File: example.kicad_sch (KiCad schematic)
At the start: 3 parts, among them J1 SSD1309 24-Pin Connector, J2 SSD1322 30-Pin Connector, J3 SSD1327 16-Pin Connector

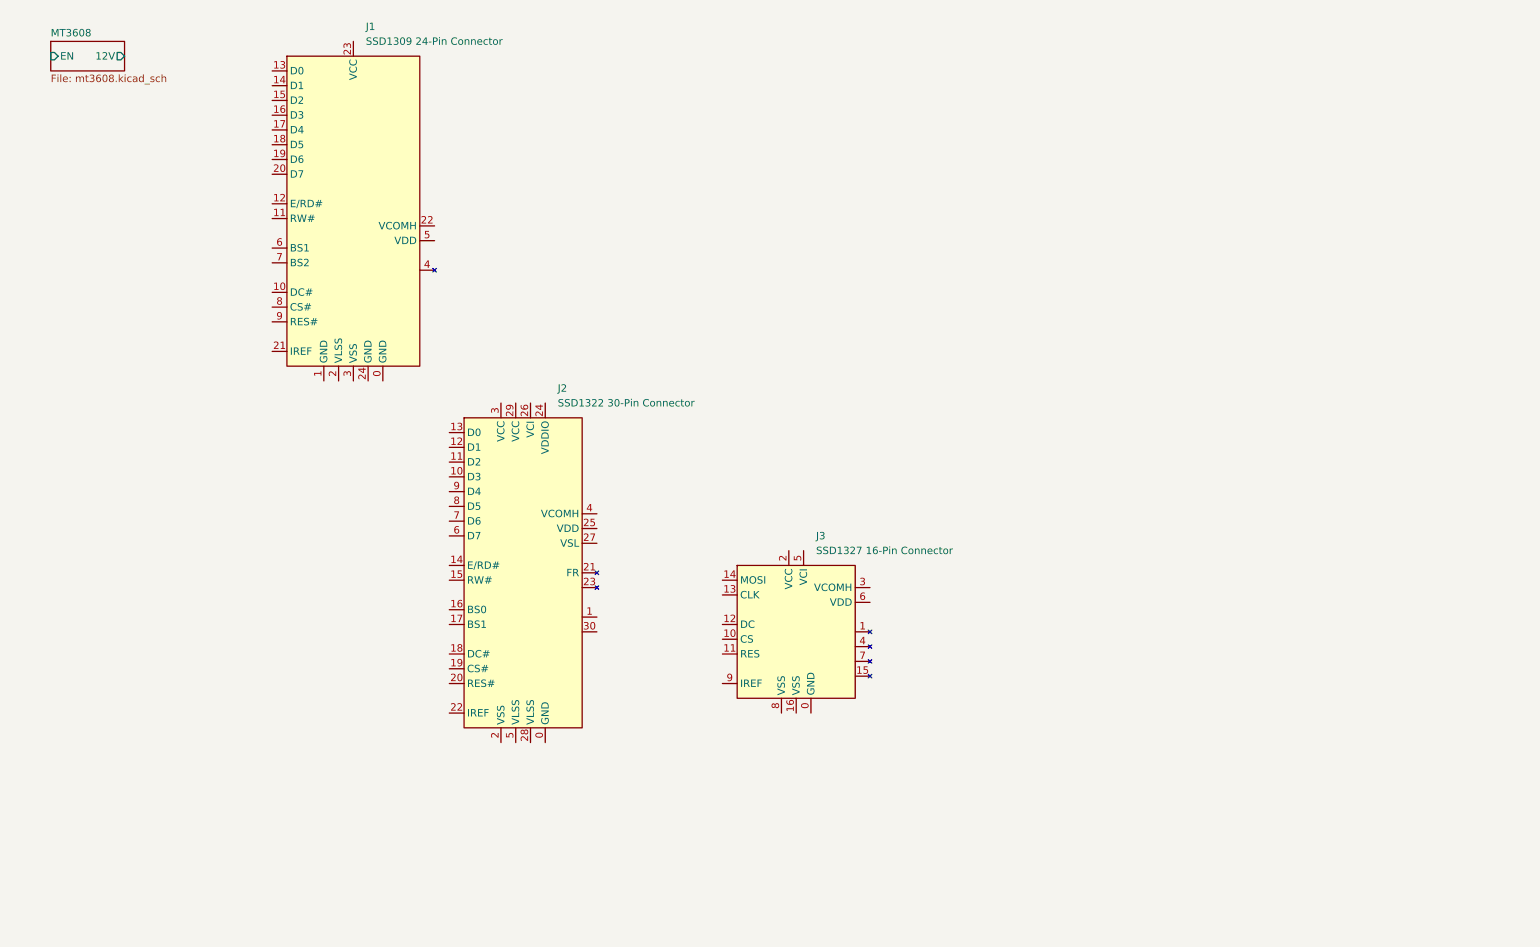
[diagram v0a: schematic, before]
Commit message: Added an example schematic for the OLED devices
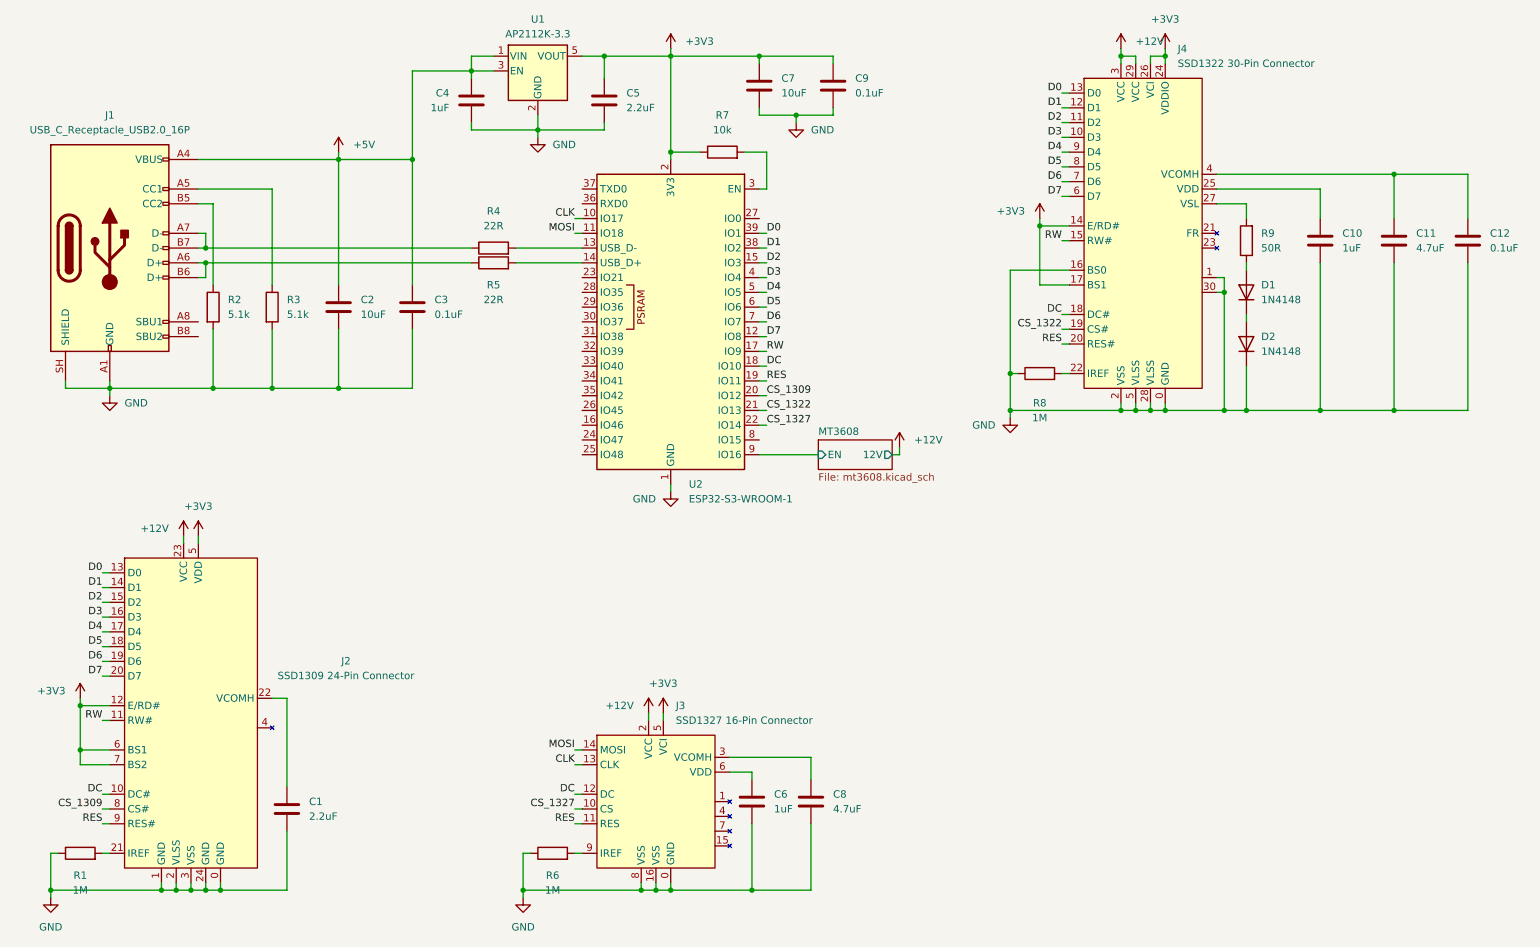
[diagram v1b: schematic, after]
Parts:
- added C1, C5: 2.2uF, Capacitor_SMD:C_0603_1608Metric, symbol Device:C
- added C10, C4, C6: 1uF, Capacitor_SMD:C_0603_1608Metric, symbol Device:C
- added C11, C8: 4.7uF, Capacitor_SMD:C_0603_1608Metric, symbol Device:C
- added C12, C3, C9: 0.1uF, Capacitor_SMD:C_0603_1608Metric, symbol Device:C
- added C2, C7: 10uF, Capacitor_SMD:C_0603_1608Metric, symbol Device:C
- added D1, D2: 1N4148, Diode_THT:D_DO-35_SOD27_P7.62mm_Horizontal, symbol Diode:1N4148
- added J1: USB_C_Receptacle_USB2.0_16P, Connector_USB:USB_C_Receptacle_HCTL_HC-TYPE-C-16P-01A, symbol Connector:USB_C_Receptacle_USB2.0_16P
- added R1, R6, R8: 1M, Resistor_SMD:R_0603_1608Metric, symbol Device:R
- added R2, R3: 5.1k, Resistor_SMD:R_0603_1608Metric, symbol Device:R
- added R4, R5: 22R, Resistor_SMD:R_0603_1608Metric, symbol Device:R
- added R7: 10k, Resistor_SMD:R_0603_1608Metric, symbol Device:R
- added R9: 50R, Resistor_SMD:R_0603_1608Metric, symbol Device:R
- added U1: AP2112K-3.3, Package_TO_SOT_SMD:SOT-23-5, symbol Regulator_Linear:AP2112K-3.3
- added U2: ESP32-S3-WROOM-1, RF_Module:ESP32-S3-WROOM-1, symbol RF_Module:ESP32-S3-WROOM-1
- renumbered J1 to J2, J2 to J4
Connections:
- net MT3608/EN: now also U2.9 (IO16)
- net GND: now reaches J2.0 (GND)
- net GND: now also J2.1 (GND), J2.2 (VLSS), J2.24 (GND), J2.3 (VSS), J3.0 (GND), J3.16 (VSS), J3.8 (VSS), J4.0 (GND), J4.1, J4.16 (BS0), J4.2 (VSS), J4.28 (VLSS), J4.30, J4.5 (VLSS), C1.2, C10.2, C11.2, C12.2, C2.2, C3.2, C4.2, C5.2, C6.2, C7.2, C8.2, C9.2, D2.1 (K), J1.A1 (GND), J1.A12 (GND), J1.B1 (GND), J1.B12 (GND), J1.SH (SHIELD), R1.1, R2.2, R3.2, R6.1, R8.1, U1.2 (GND), U2.1 (GND), U2.40 (GND), U2.41 (GND)
- net DC: now reaches J2.10 (DC#)
- net DC: now also J3.12 (DC), J4.18 (DC#), U2.18 (IO10)
- net RW: now reaches J2.11 (RW#)
- net RW: now also J4.15 (RW#), U2.17 (IO9)
- net +3V3: now reaches J2.12 (E/RD#)
- net +3V3: now also J2.5 (VDD), J2.6 (BS1), J2.7 (BS2), J3.5 (VCI), J4.14 (E/RD#), J4.17 (BS1), J4.24 (VDDIO), J4.26 (VCI), C5.1, C7.1, C9.1, R7.1, U1.5 (VOUT), U2.2 (3V3)
- net D0: now reaches J2.13 (D0)
- net D0: now also J4.13 (D0), U2.39 (IO1)
- net D1: now reaches J2.14 (D1)
- net D1: now also J4.12 (D1), U2.38 (IO2)
- net D2: now reaches J2.15 (D2)
- net D2: now also J4.11 (D2), U2.15 (IO3)
- net D3: now reaches J2.16 (D3)
- net D3: now also J4.10 (D3), U2.4 (IO4)
- net D4: now reaches J2.17 (D4)
- net D4: now also J4.9 (D4), U2.5 (IO5)
- net D5: now reaches J2.18 (D5)
- net D5: now also J4.8 (D5), U2.6 (IO6)
- net D6: now reaches J2.19 (D6)
- net D6: now also J4.7 (D6), U2.7 (IO7)
- net D7: now reaches J2.20 (D7)
- net D7: now also J4.6 (D7), U2.12 (IO8)
- net at J2.21 (IREF): now also R1.2
- net at J2.22 (VCOMH): now also C1.1
- net +12V: now reaches J2.23 (VCC)
- net +12V: now also J3.2 (VCC), J4.29 (VCC), J4.3 (VCC)
- net CS_1309: now reaches J2.8 (CS#)
- net CS_1309: now also U2.20 (IO12)
- net RES: now reaches J2.9 (RES#)
- net RES: now also J3.11 (RES), J4.20 (RES#), U2.19 (IO11)
- net CS_1322: now reaches J4.19 (CS#)
- net CS_1322: now also U2.21 (IO13)
- net at J4.22 (IREF): now also R8.2
- net at J4.25 (VDD): now also C10.1
- net at J4.27 (VSL): now also R9.2
- net at J4.4 (VCOMH): now also C11.1, C12.1
- net CS_1327: now reaches J3.10 (CS)
- net CS_1327: now also U2.22 (IO14)
- net CLK: now reaches J3.13 (CLK)
- net CLK: now also U2.10 (IO17)
- net MOSI: now reaches J3.14 (MOSI)
- net MOSI: now also U2.11 (IO18)
- net at J3.3 (VCOMH): now also C8.1
- net at J3.6 (VDD): now also C6.1
- net at J3.9 (IREF): now also R6.2
- new net: D1.1 (K), D2.2 (A)
- new net: D1.2 (A), R9.1
- new net: J1.A5 (CC1), R3.1
- new net: J1.A6 (D+), J1.B6 (D+), R5.1
- new net: J1.A7 (D-), J1.B7 (D-), R4.1
- new net: J1.B5 (CC2), R2.1
- new net: R5.2, U2.14 (USB_D+)
- new net: R4.2, U2.13 (USB_D-)
- new net: R7.2, U2.3 (EN)
- new net +5V: C2.1, C3.1, C4.1, J1.A4 (VBUS), J1.A9 (VBUS), J1.B4 (VBUS), J1.B9 (VBUS), U1.1 (VIN), U1.3 (EN)
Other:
- moved on the sheet: J2, J3, J4

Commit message: PCB layout part 1
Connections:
- net CLK: now also U2.32 (IO39); no longer U2.10 (IO17)
- net CS_1309: now also U2.12 (IO8); no longer U2.20 (IO12)
- net CS_1322: now also U2.15 (IO3); no longer U2.21 (IO13)
- net CS_1327: now also U2.33 (IO40); no longer U2.22 (IO14)
- net D0: now also U2.19 (IO11); no longer U2.39 (IO1)
- net D1: now also U2.20 (IO12); no longer U2.38 (IO2)
- net D2: now also U2.21 (IO13); no longer U2.15 (IO3)
- net D3: now also U2.22 (IO14); no longer U2.4 (IO4)
- net D4: now also U2.23 (IO21); no longer U2.5 (IO5)
- net D5: now also U2.24 (IO47); no longer U2.6 (IO6)
- net D6: now also U2.25 (IO48); no longer U2.7 (IO7)
- net D7: now also U2.26 (IO45); no longer U2.12 (IO8)
- net DC: now also U2.17 (IO9); no longer U2.18 (IO10)
- net MOSI: now also U2.31 (IO38); no longer U2.11 (IO18)
- net RES: now also U2.16 (IO46); no longer U2.19 (IO11)
- net RW: now also U2.18 (IO10); no longer U2.17 (IO9)

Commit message: PCB layout part 2
Really dense layout but incomplete; can't connect GND nodes
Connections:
- net MT3608/EN: now also U2.34 (IO41); no longer U2.9 (IO16)
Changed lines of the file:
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@@
 	(wire
 		(pts
-			(xy 170.18 96.52) (xy 171.45 96.52)
+			(xy 104.14 81.28) (xy 105.41 81.28)
 		)
 		(stroke
@@
 	(wire
 		(pts
-			(xy 147.32 96.52) (xy 157.48 96.52)
-		)
-		(stroke
-			(width 0)
-			(type default)
-		)
-	)
-	(wire
-		(pts
 			(xy 30.48 147.32) (xy 35.56 147.32)
 		)
@@
 	(wire
 		(pts
+			(xy 104.14 83.82) (xy 116.84 83.82)
+		)
+		(stroke
+			(width 0)
+			(type default)
+		)
+	)
+	(wire
+		(pts
 			(xy 115.57 76.2) (xy 116.84 76.2)
 		)
@@
 	(wire
 		(pts
-			(xy 171.45 96.52) (xy 171.45 95.25)
+			(xy 105.41 81.28) (xy 105.41 80.01)
 		)
 		(stroke
@@
 		)
 		(property "Value" "+3V3"
-			(at 50.8 105.41 0)
+			(at 53.34 109.2199 0)
 			(show_name no)
 			(do_not_autoplace no)
@@
 					(size 1.27 1.27)
 				)
+				(justify left)
 			)
 		)
@@
 		)
 		(property "Value" "+12V"
-			(at 45.72 109.2199 0)
+			(at 48.26 105.41 0)
 			(show_name no)
 			(do_not_autoplace no)
@@
 					(size 1.27 1.27)
 				)
-				(justify right)
 			)
 		)
@@
 		)
 		(property "Value" "GND"
-			(at 25.4 177.8 0)
+			(at 27.94 173.9899 0)
 			(show_name no)
 			(do_not_autoplace no)
@@
 					(size 1.27 1.27)
 				)
+				(justify left)
 			)
 		)
@@
 		)
 		(property "Value" "GND"
-			(at 106.68 177.8 0)
+			(at 109.22 173.9899 0)
 			(show_name no)
 			(do_not_autoplace no)
@@
 					(size 1.27 1.27)
 				)
+				(justify left)
 			)
 		)
@@
 	(symbol
 		(lib_id "power:+12V")
-		(at 171.45 95.25 0)
+		(at 105.41 80.01 0)
 		(unit 1)
 		(body_style 1)
@@
 		(fields_autoplaced yes)
 		(property "Reference" "#PWR014"
-			(at 171.45 99.06 0)
+			(at 105.41 83.82 0)
 			(hide yes)
 			(show_name no)
@@
 		)
 		(property "Value" "+12V"
-			(at 173.99 93.9799 0)
+			(at 107.95 78.7399 0)
 			(show_name no)
 			(do_not_autoplace no)
@@
 		)
 		(property "Footprint" ""
-			(at 171.45 95.25 0)
+			(at 105.41 80.01 0)
 			(hide yes)
 			(show_name no)
@@
 		)
 		(property "Datasheet" ""
-			(at 171.45 95.25 0)
+			(at 105.41 80.01 0)
 			(hide yes)
 			(show_name no)
@@
 		)
 		(property "Description" "Power symbol creates a global label with name \"+12V\""
-			(at 171.45 95.25 0)
+			(at 105.41 80.01 0)
 			(hide yes)
 			(show_name no)
@@
 	)
 	(sheet
-		(at 157.48 93.98)
-		(size 12.7 5.08)
+		(at 91.44 78.74)
+		(size 12.7 7.62)
 		(exclude_from_sim no)
 		(in_bom yes)
@@
 		)
 		(property "Sheetname" "MT3608"
-			(at 157.48 93.2684 0)
+			(at 91.44 78.0284 0)
 			(show_name no)
 			(do_not_autoplace no)
@@
 		)
 		(property "Sheetfile" "mt3608.kicad_sch"
-			(at 157.48 99.6446 0)
+			(at 91.44 86.9446 0)
 			(show_name no)
 			(do_not_autoplace no)
@@
 		)
 		(pin "EN" input
-			(at 157.48 96.52 180)
+			(at 104.14 83.82 0)
 			(effects
 				(font
 					(size 1.27 1.27)
 				)
-				(justify left)
+				(justify right)
 			)
 		)
 		(pin "12V" output
-			(at 170.18 96.52 0)
+			(at 104.14 81.28 0)
 			(effects
 				(font

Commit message: PCB layout part 3
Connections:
- net CS_1322: now also U2.16 (IO46); no longer U2.15 (IO3)
- net MT3608/EN: now also U2.11 (IO18); no longer U2.34 (IO41)
- net RES: now also U2.15 (IO3); no longer U2.16 (IO46)
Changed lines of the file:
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@@
 	(wire
 		(pts
-			(xy 104.14 81.28) (xy 105.41 81.28)
+			(xy 107.95 49.53) (xy 109.22 49.53)
 		)
 		(stroke
@@
 	(wire
 		(pts
-			(xy 104.14 83.82) (xy 116.84 83.82)
-		)
-		(stroke
-			(width 0)
-			(type default)
-		)
-	)
-	(wire
-		(pts
 			(xy 115.57 76.2) (xy 116.84 76.2)
 		)
@@
 	(wire
 		(pts
+			(xy 113.03 52.07) (xy 113.03 58.42)
+		)
+		(stroke
+			(width 0)
+			(type default)
+		)
+	)
+	(wire
+		(pts
 			(xy 34.29 129.54) (xy 35.56 129.54)
 		)
@@
 	(wire
 		(pts
+			(xy 107.95 52.07) (xy 113.03 52.07)
+		)
+		(stroke
+			(width 0)
+			(type default)
+		)
+	)
+	(wire
+		(pts
 			(xy 106.68 171.45) (xy 106.68 172.72)
 		)
@@
 	(wire
 		(pts
+			(xy 113.03 58.42) (xy 116.84 58.42)
+		)
+		(stroke
+			(width 0)
+			(type default)
+		)
+	)
+	(wire
+		(pts
 			(xy 190.5 88.9) (xy 209.55 88.9)
 		)
@@
 	(wire
 		(pts
-			(xy 105.41 81.28) (xy 105.41 80.01)
+			(xy 109.22 49.53) (xy 109.22 48.26)
 		)
 		(stroke
@@
 		)
 	)
-	(label "CS_1322"
-		(at 148.59 63.5 0)
-		(effects
-			(font
-				(size 1.27 1.27)
-			)
-			(justify left bottom)
-		)
-	)
 	(label "D5"
 		(at 199.39 46.99 180)
@@
 		)
 	)
-	(label "RES"
+	(label "CS_1322"
 		(at 115.57 91.44 180)
 		(effects
@@
 		)
 	)
+	(label "RES"
+		(at 148.59 63.5 0)
+		(effects
+			(font
+				(size 1.27 1.27)
+			)
+			(justify left bottom)
+		)
+	)
 	(label "D5"
 		(at 34.29 129.54 180)
@@
 	(symbol
 		(lib_id "power:+12V")
-		(at 105.41 80.01 0)
+		(at 109.22 48.26 0)
 		(unit 1)
 		(body_style 1)
@@
 		(fields_autoplaced yes)
 		(property "Reference" "#PWR014"
-			(at 105.41 83.82 0)
+			(at 109.22 52.07 0)
 			(hide yes)
 			(show_name no)
@@
 		)
 		(property "Value" "+12V"
-			(at 107.95 78.7399 0)
+			(at 111.76 46.9899 0)
 			(show_name no)
 			(do_not_autoplace no)
@@
 		)
 		(property "Footprint" ""
-			(at 105.41 80.01 0)
+			(at 109.22 48.26 0)
 			(hide yes)
 			(show_name no)
@@
 		)
 		(property "Datasheet" ""
-			(at 105.41 80.01 0)
+			(at 109.22 48.26 0)
 			(hide yes)
 			(show_name no)
@@
 		)
 		(property "Description" "Power symbol creates a global label with name \"+12V\""
-			(at 105.41 80.01 0)
+			(at 109.22 48.26 0)
 			(hide yes)
 			(show_name no)
@@
 	)
 	(sheet
-		(at 91.44 78.74)
+		(at 95.25 46.99)
 		(size 12.7 7.62)
 		(exclude_from_sim no)
@@
 		)
 		(property "Sheetname" "MT3608"
-			(at 91.44 78.0284 0)
+			(at 95.25 46.2784 0)
 			(show_name no)
 			(do_not_autoplace no)
@@
 		)
 		(property "Sheetfile" "mt3608.kicad_sch"
-			(at 91.44 86.9446 0)
+			(at 95.25 55.1946 0)
 			(show_name no)
 			(do_not_autoplace no)
@@
 		)
 		(pin "EN" input
-			(at 104.14 83.82 0)
+			(at 107.95 52.07 0)
 			(effects
 				(font
@@
 		)
 		(pin "12V" output
-			(at 104.14 81.28 0)
+			(at 107.95 49.53 0)
 			(effects
 				(font

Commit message: PCB layout part 4
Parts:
- D1, D2: footprint Diode_THT:D_DO-35_SOD27_P7.62mm_Horizontal -> Diode_SMD:D_SOD-123
- U2: now left out of the parts list
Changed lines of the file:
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@@
 			)
 		)
-		(property "Footprint" "Diode_THT:D_DO-35_SOD27_P7.62mm_Horizontal"
+		(property "Footprint" "Diode_SMD:D_SOD-123"
 			(at 231.14 68.58 0)
 			(hide yes)
@@
 		(body_style 1)
 		(exclude_from_sim no)
-		(in_bom yes)
+		(in_bom no)
 		(on_board yes)
 		(in_pos_files yes)
@@
 			)
 		)
-		(property "Footprint" "Diode_THT:D_DO-35_SOD27_P7.62mm_Horizontal"
+		(property "Footprint" "Diode_SMD:D_SOD-123"
 			(at 231.14 77.47 0)
 			(hide yes)
